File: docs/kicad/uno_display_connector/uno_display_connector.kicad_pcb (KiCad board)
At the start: 2 copper layers, 3 parts, among them J1 Conn_01x08, J2 Conn_01x08, U1 uno_display

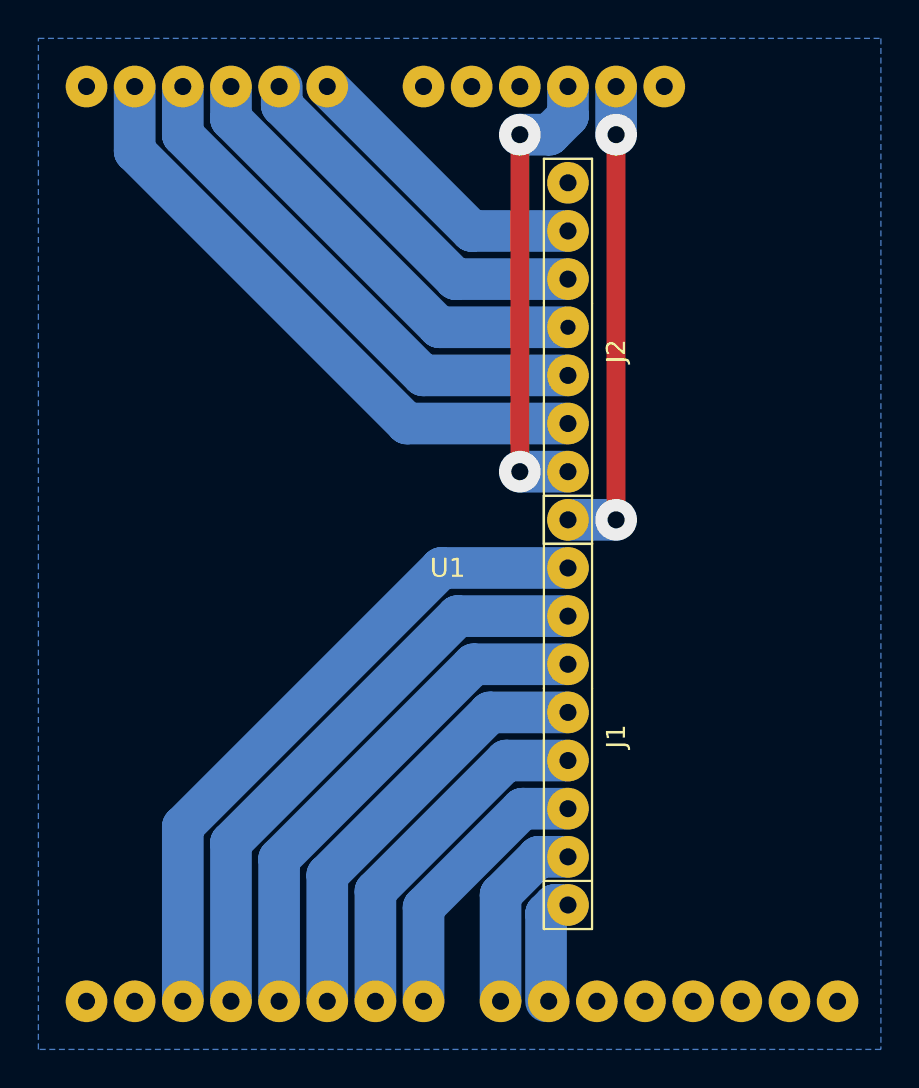
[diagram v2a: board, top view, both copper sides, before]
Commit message: BUILD new combined mother_board and uno_display_connector. PRINT new display_frame.
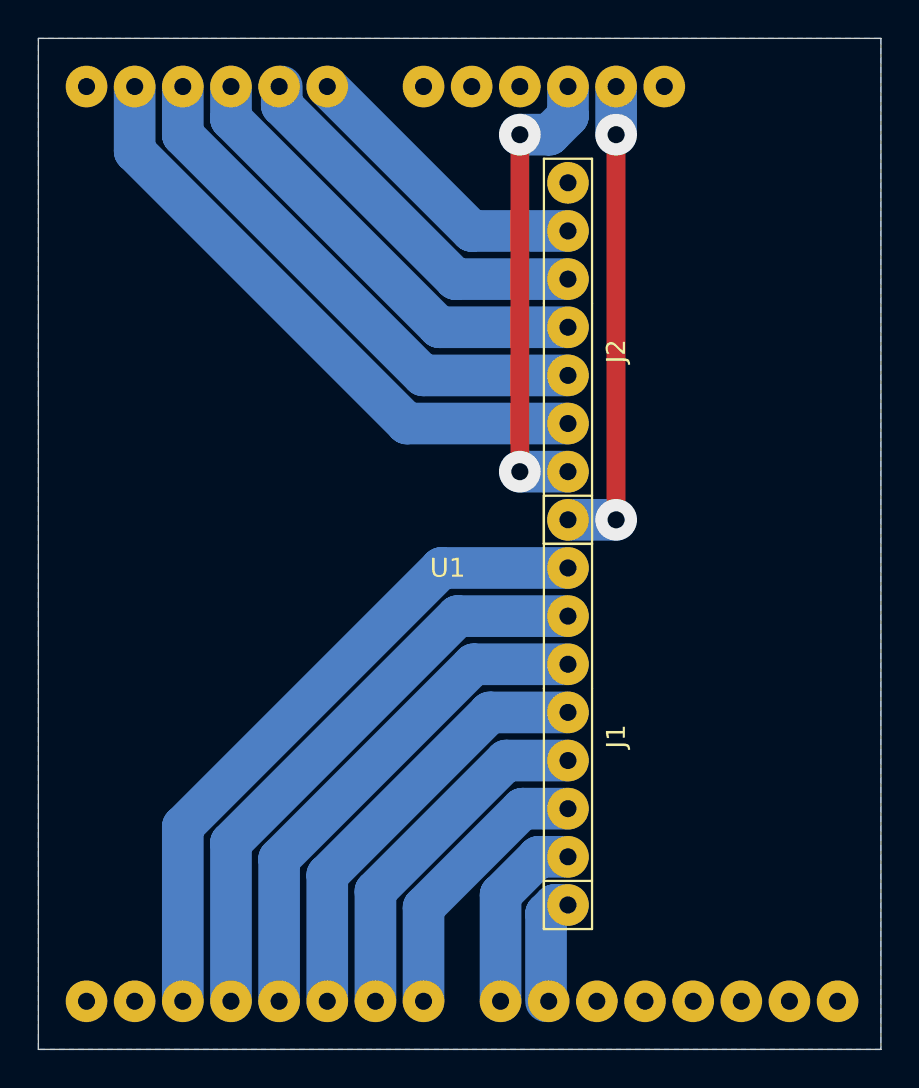
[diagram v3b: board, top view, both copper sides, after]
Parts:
- J1, J2: footprint cnc3018-PCB:my8Pin -> 0_my_footprints:my8Pin
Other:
- board outline added: 44.5 x 53.3 mm
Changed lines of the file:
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@@
   (general
     (thickness 1.6)
-    (drawings 1)
+    (drawings 7)
     (tracks 52)
     (zones 0)
@@
     (add_net "Net-(U1-Pad28)")
   )
-  (module cnc3018-PCB:my8Pin (layer F.Cu)
+  (module 0_my_footprints:my8Pin (layer F.Cu)
     (at 27.94 -15.24 90)
     (fp_text reference J1 (at 1.27 2.54 90) (layer F.SilkS)
@@
     (fp_line (start -8.89 -1.27) (end -6.35 -1.27) (layer F.SilkS) (width 0.12))
     (fp_line (start -6.35 -1.27) (end -6.35 1.27) (layer F.SilkS) (width 0.12))
+    (pad 8 thru_hole circle (at 10.16 0 90) (size 2.2 2.2) (drill 0.9) (layers *.Cu *.Mask)
+      (net 8 LCD_D2))
+    (pad 7 thru_hole circle (at 7.62 0 90) (size 2.2 2.2) (drill 0.9) (layers *.Cu *.Mask)
+      (net 7 LCD_D3))
+    (pad 6 thru_hole circle (at 5.08 0 90) (size 2.2 2.2) (drill 0.9) (layers *.Cu *.Mask)
+      (net 6 LCD_D4))
+    (pad 5 thru_hole circle (at 2.54 0 90) (size 2.2 2.2) (drill 0.9) (layers *.Cu *.Mask)
+      (net 5 LCD_D5))
+    (pad 4 thru_hole circle (at 0 0 90) (size 2.2 2.2) (drill 0.9) (layers *.Cu *.Mask)
+      (net 4 LCD_D6))
+    (pad 3 thru_hole circle (at -2.54 0 90) (size 2.2 2.2) (drill 0.9) (layers *.Cu *.Mask)
+      (net 3 LCD_D7))
+    (pad 2 thru_hole circle (at -5.08 0 90) (size 2.2 2.2) (drill 0.9) (layers *.Cu *.Mask)
+      (net 2 LCD_D0))
     (pad 1 thru_hole circle (at -7.62 0 90) (size 2.2 2.2) (drill 0.9) (layers *.Cu *.Mask)
       (net 1 LCD_D1))
-    (pad 2 thru_hole circle (at -5.08 0 90) (size 2.2 2.2) (drill 0.9) (layers *.Cu *.Mask)
-      (net 2 LCD_D0))
-    (pad 3 thru_hole circle (at -2.54 0 90) (size 2.2 2.2) (drill 0.9) (layers *.Cu *.Mask)
-      (net 3 LCD_D7))
-    (pad 4 thru_hole circle (at 0 0 90) (size 2.2 2.2) (drill 0.9) (layers *.Cu *.Mask)
-      (net 4 LCD_D6))
-    (pad 5 thru_hole circle (at 2.54 0 90) (size 2.2 2.2) (drill 0.9) (layers *.Cu *.Mask)
-      (net 5 LCD_D5))
-    (pad 6 thru_hole circle (at 5.08 0 90) (size 2.2 2.2) (drill 0.9) (layers *.Cu *.Mask)
-      (net 6 LCD_D4))
-    (pad 7 thru_hole circle (at 7.62 0 90) (size 2.2 2.2) (drill 0.9) (layers *.Cu *.Mask)
-      (net 7 LCD_D3))
-    (pad 8 thru_hole circle (at 10.16 0 90) (size 2.2 2.2) (drill 0.9) (layers *.Cu *.Mask)
-      (net 8 LCD_D2))
-  )
-  (module cnc3018-PCB:my8Pin (layer F.Cu)
+  )
+  (module 0_my_footprints:my8Pin (layer F.Cu)
     (at 27.94 -35.56 90)
     (fp_text reference J2 (at 1.27 2.54 90) (layer F.SilkS)
@@
       (effects (font (size 1 1) (thickness 0.15)))
     )
+    (fp_line (start 11.43 1.27) (end 3.81 1.27) (layer F.SilkS) (width 0.12))
+    (fp_line (start 11.43 -1.27) (end 11.43 1.27) (layer F.SilkS) (width 0.12))
+    (fp_line (start 3.81 -1.27) (end 11.43 -1.27) (layer F.SilkS) (width 0.12))
+    (fp_line (start -8.89 -1.27) (end -8.89 1.27) (layer F.SilkS) (width 0.12))
+    (fp_line (start -8.89 1.27) (end 3.81 1.27) (layer F.SilkS) (width 0.12))
+    (fp_line (start 3.81 -1.27) (end -8.89 -1.27) (layer F.SilkS) (width 0.12))
+    (fp_line (start -8.89 -1.27) (end -6.35 -1.27) (layer F.SilkS) (width 0.12))
     (fp_line (start -6.35 -1.27) (end -6.35 1.27) (layer F.SilkS) (width 0.12))
-    (fp_line (start -8.89 -1.27) (end -6.35 -1.27) (layer F.SilkS) (width 0.12))
-    (fp_line (start 3.81 -1.27) (end -8.89 -1.27) (layer F.SilkS) (width 0.12))
-    (fp_line (start -8.89 1.27) (end 3.81 1.27) (layer F.SilkS) (width 0.12))
-    (fp_line (start -8.89 -1.27) (end -8.89 1.27) (layer F.SilkS) (width 0.12))
-    (fp_line (start 3.81 -1.27) (end 11.43 -1.27) (layer F.SilkS) (width 0.12))
-    (fp_line (start 11.43 -1.27) (end 11.43 1.27) (layer F.SilkS) (width 0.12))
-    (fp_line (start 11.43 1.27) (end 3.81 1.27) (layer F.SilkS) (width 0.12))
     (pad 8 thru_hole circle (at 10.16 0 90) (size 2.2 2.2) (drill 0.9) (layers *.Cu *.Mask)
       (net 9 GND))
@@
     (pad 6 thru_hole circle (at 5.08 0 90) (size 2.2 2.2) (drill 0.9) (layers *.Cu *.Mask)
       (net 12 LCD_WR))
-    (pad 5 thru_hole circle (at 2.54 0 90) (size 2.2 2.2) (drill 0.8) (layers *.Cu *.Mask)
+    (pad 5 thru_hole circle (at 2.54 0 90) (size 2.2 2.2) (drill 0.9) (layers *.Cu *.Mask)
       (net 13 LCD_RS))
     (pad 4 thru_hole circle (at 0 0 90) (size 2.2 2.2) (drill 0.9) (layers *.Cu *.Mask)
@@
     )
   )
+  (gr_line (start 44.45 -53.34) (end 0 -53.34) (layer Edge.Cuts) (width 0.05))
+  (gr_line (start 44.45 0) (end 44.45 -53.34) (layer Edge.Cuts) (width 0.05))
+  (gr_line (start 0 0) (end 44.45 0) (layer Edge.Cuts) (width 0.05))
+  (gr_line (start 0 -53.34) (end 0 0) (layer Edge.Cuts) (width 0.05))
+  (dimension 53.34 (width 0.15) (layer Dwgs.User)
+    (gr_text "53.340 mm" (at -13.364999 -26.67 270) (layer Dwgs.User)
+      (effects (font (size 1 1) (thickness 0.15)))
+    )
+    (feature1 (pts (xy 0 0) (xy -12.65142 0)))
+    (feature2 (pts (xy 0 -53.34) (xy -12.65142 -53.34)))
+    (crossbar (pts (xy -12.064999 -53.34) (xy -12.064999 0)))
+    (arrow1a (pts (xy -12.064999 0) (xy -12.65142 -1.126504)))
+    (arrow1b (pts (xy -12.064999 0) (xy -11.478578 -1.126504)))
+    (arrow2a (pts (xy -12.064999 -53.34) (xy -12.65142 -52.213496)))
+    (arrow2b (pts (xy -12.064999 -53.34) (xy -11.478578 -52.213496)))
+  )
+  (dimension 44.45 (width 0.15) (layer Dwgs.User)
+    (gr_text "44.450 mm" (at 22.225 7.014999) (layer Dwgs.User)
+      (effects (font (size 1 1) (thickness 0.15)))
+    )
+    (feature1 (pts (xy 44.45 0) (xy 44.45 6.30142)))
+    (feature2 (pts (xy 0 0) (xy 0 6.30142)))
+    (crossbar (pts (xy 0 5.714999) (xy 44.45 5.714999)))
+    (arrow1a (pts (xy 44.45 5.714999) (xy 43.323496 6.30142)))
+    (arrow1b (pts (xy 44.45 5.714999) (xy 43.323496 5.128578)))
+    (arrow2a (pts (xy 0 5.714999) (xy 1.126504 6.30142)))
+    (arrow2b (pts (xy 0 5.714999) (xy 1.126504 5.128578)))
+  )
   (gr_text "NOTE that LCD_D0 and LCD_D1 are switched\nwhile soldering the wires onto this connector so  \nALL DATA LINES COME OUT IN ORDER on the\nother end as REQUIRED by the mother board!!!" (at 35.56 -17.145) (layer Dwgs.User)

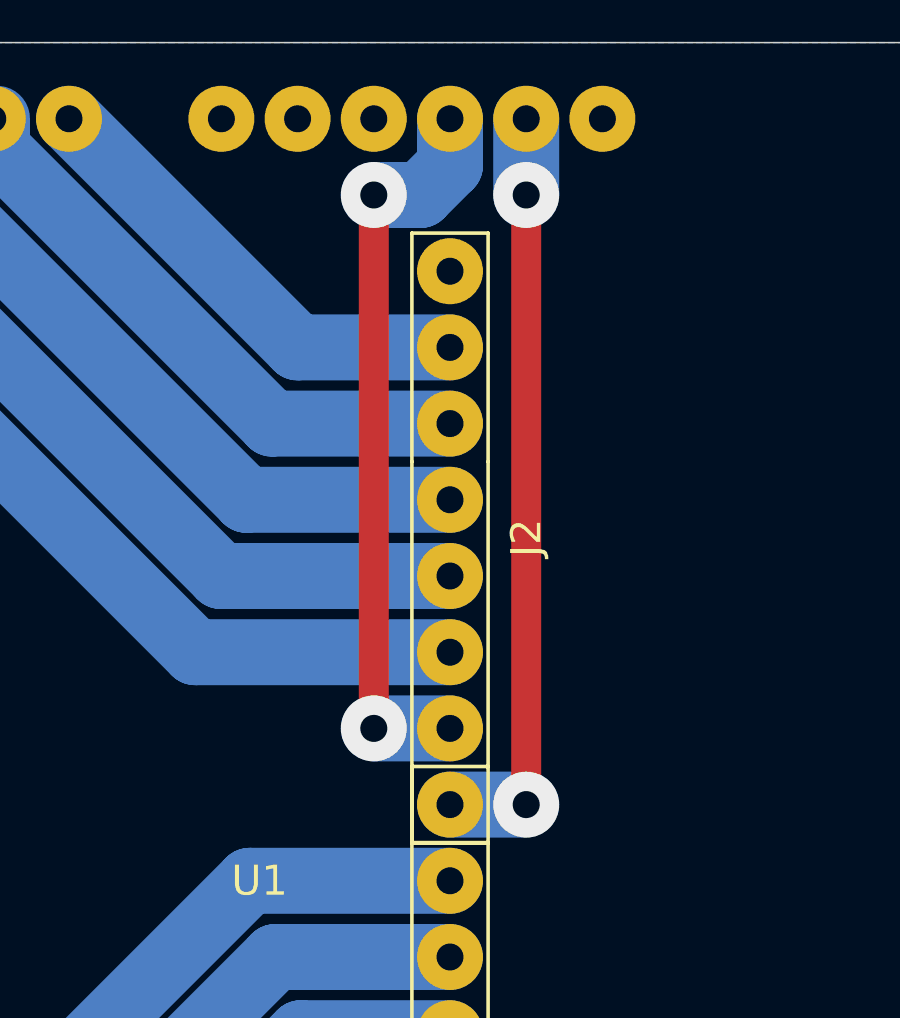
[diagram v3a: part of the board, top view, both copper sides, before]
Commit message: AFTER BUILD NEW PCBs - corrected display connector pins; removed old combined plot and gcode file
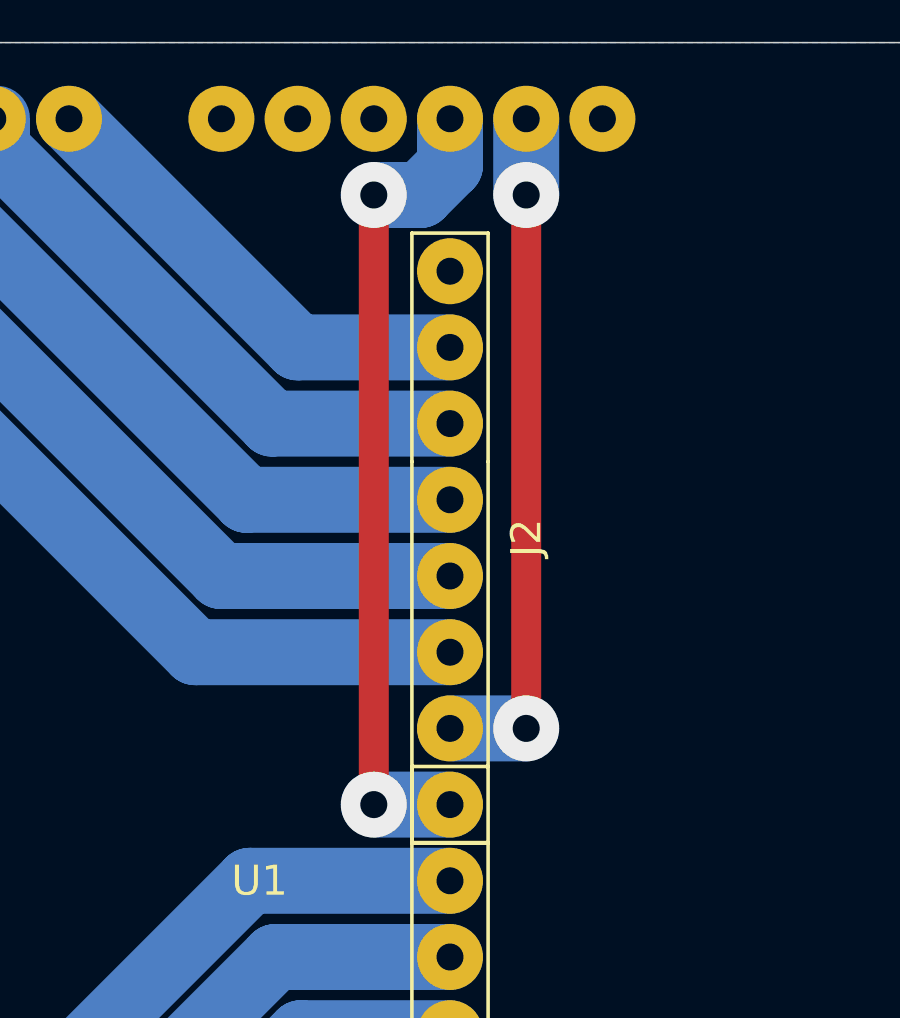
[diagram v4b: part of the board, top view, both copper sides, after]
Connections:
- J2 pad 1: +3V3 -> +5V
- J2 pad 2: +5V -> +3V3
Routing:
- net +5V: track 24.8 -> 27.4 mm
- net +3V3: track 25.4 -> 22.9 mm
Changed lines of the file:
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@@
   )
   (setup
-    (last_trace_width 0.25)
+    (last_trace_width 1)
     (user_trace_width 1)
     (user_trace_width 2)
@@
       (effects (font (size 1 1) (thickness 0.15)))
     )
+    (fp_line (start -6.35 -1.27) (end -6.35 1.27) (layer F.SilkS) (width 0.12))
+    (fp_line (start -8.89 -1.27) (end -6.35 -1.27) (layer F.SilkS) (width 0.12))
+    (fp_line (start 3.81 -1.27) (end -8.89 -1.27) (layer F.SilkS) (width 0.12))
+    (fp_line (start -8.89 1.27) (end 3.81 1.27) (layer F.SilkS) (width 0.12))
+    (fp_line (start -8.89 -1.27) (end -8.89 1.27) (layer F.SilkS) (width 0.12))
+    (fp_line (start 3.81 -1.27) (end 11.43 -1.27) (layer F.SilkS) (width 0.12))
+    (fp_line (start 11.43 -1.27) (end 11.43 1.27) (layer F.SilkS) (width 0.12))
     (fp_line (start 11.43 1.27) (end 3.81 1.27) (layer F.SilkS) (width 0.12))
-    (fp_line (start 11.43 -1.27) (end 11.43 1.27) (layer F.SilkS) (width 0.12))
-    (fp_line (start 3.81 -1.27) (end 11.43 -1.27) (layer F.SilkS) (width 0.12))
-    (fp_line (start -8.89 -1.27) (end -8.89 1.27) (layer F.SilkS) (width 0.12))
-    (fp_line (start -8.89 1.27) (end 3.81 1.27) (layer F.SilkS) (width 0.12))
-    (fp_line (start 3.81 -1.27) (end -8.89 -1.27) (layer F.SilkS) (width 0.12))
-    (fp_line (start -8.89 -1.27) (end -6.35 -1.27) (layer F.SilkS) (width 0.12))
-    (fp_line (start -6.35 -1.27) (end -6.35 1.27) (layer F.SilkS) (width 0.12))
     (pad 8 thru_hole circle (at 10.16 0 90) (size 2.2 2.2) (drill 0.9) (layers *.Cu *.Mask)
       (net 8 LCD_D2))
@@
       (effects (font (size 1 1) (thickness 0.15)))
     )
+    (fp_line (start -6.35 -1.27) (end -6.35 1.27) (layer F.SilkS) (width 0.12))
+    (fp_line (start -8.89 -1.27) (end -6.35 -1.27) (layer F.SilkS) (width 0.12))
+    (fp_line (start 3.81 -1.27) (end -8.89 -1.27) (layer F.SilkS) (width 0.12))
+    (fp_line (start -8.89 1.27) (end 3.81 1.27) (layer F.SilkS) (width 0.12))
+    (fp_line (start -8.89 -1.27) (end -8.89 1.27) (layer F.SilkS) (width 0.12))
+    (fp_line (start 3.81 -1.27) (end 11.43 -1.27) (layer F.SilkS) (width 0.12))
+    (fp_line (start 11.43 -1.27) (end 11.43 1.27) (layer F.SilkS) (width 0.12))
     (fp_line (start 11.43 1.27) (end 3.81 1.27) (layer F.SilkS) (width 0.12))
-    (fp_line (start 11.43 -1.27) (end 11.43 1.27) (layer F.SilkS) (width 0.12))
-    (fp_line (start 3.81 -1.27) (end 11.43 -1.27) (layer F.SilkS) (width 0.12))
-    (fp_line (start -8.89 -1.27) (end -8.89 1.27) (layer F.SilkS) (width 0.12))
-    (fp_line (start -8.89 1.27) (end 3.81 1.27) (layer F.SilkS) (width 0.12))
-    (fp_line (start 3.81 -1.27) (end -8.89 -1.27) (layer F.SilkS) (width 0.12))
-    (fp_line (start -8.89 -1.27) (end -6.35 -1.27) (layer F.SilkS) (width 0.12))
-    (fp_line (start -6.35 -1.27) (end -6.35 1.27) (layer F.SilkS) (width 0.12))
     (pad 8 thru_hole circle (at 10.16 0 90) (size 2.2 2.2) (drill 0.9) (layers *.Cu *.Mask)
       (net 9 GND))
@@
       (net 15 LCD_RST))
     (pad 2 thru_hole circle (at -5.08 0 90) (size 2.2 2.2) (drill 0.9) (layers *.Cu *.Mask)
+      (net 10 +3V3))
+    (pad 1 thru_hole circle (at -7.62 0 90) (size 2.2 2.2) (drill 0.9) (layers *.Cu *.Mask)
       (net 16 +5V))
-    (pad 1 thru_hole circle (at -7.62 0 90) (size 2.2 2.2) (drill 0.9) (layers *.Cu *.Mask)
-      (net 10 +3V3))
   )
   (module 0_my_footprints:unoDisplay (layer F.Cu)
@@
       (effects (font (size 1 1) (thickness 0.15)))
     )
+    (fp_line (start -22.86 -27.94) (end -22.86 25.4) (layer F.Fab) (width 0.12))
+    (fp_line (start -22.86 -27.94) (end 21.59 -27.94) (layer F.Fab) (width 0.12))
+    (fp_line (start 21.59 -27.94) (end 21.59 25.4) (layer F.Fab) (width 0.12))
     (fp_line (start -22.86 25.4) (end 21.59 25.4) (layer F.Fab) (width 0.12))
-    (fp_line (start 21.59 -27.94) (end 21.59 25.4) (layer F.Fab) (width 0.12))
-    (fp_line (start -22.86 -27.94) (end 21.59 -27.94) (layer F.Fab) (width 0.12))
-    (fp_line (start -22.86 -27.94) (end -22.86 25.4) (layer F.Fab) (width 0.12))
     (pad 1 thru_hole circle (at 19.05 -25.4) (size 2.2 2.2) (drill 0.9) (layers *.Cu *.Mask)
       (net 17 "Net-(U1-Pad1)"))
@@
   (segment (start 21.25961 -25.4) (end 27.94 -25.4) (width 2.2) (layer B.Cu) (net 8))
   (segment (start 30.48 -50.8) (end 30.48 -48.26) (width 2.2) (layer B.Cu) (net 10))
-  (segment (start 27.94 -27.94) (end 30.48 -27.94) (width 2.2) (layer B.Cu) (net 10))
-  (via (at 30.48 -27.94) (size 2.2) (drill 0.9) (layers F.Cu B.Cu) (net 10))
+  (segment (start 27.94 -30.48) (end 30.48 -30.48) (width 2.2) (layer B.Cu) (net 10))
+  (via (at 30.48 -30.48) (size 2.2) (drill 0.9) (layers F.Cu B.Cu) (net 10))
   (segment (start 30.48 -48.26) (end 30.48 -48.26) (width 2.2) (layer B.Cu) (net 10))
   (via (at 30.48 -48.26) (size 2.2) (drill 0.9) (layers F.Cu B.Cu) (net 10))
-  (segment (start 30.48 -48.26) (end 30.48 -27.94) (width 1) (layer F.Cu) (net 10))
+  (segment (start 30.48 -30.48) (end 30.48 -48.26) (width 1) (layer F.Cu) (net 10))
   (segment (start 27.94 -43.18) (end 22.86 -43.18) (width 2.2) (layer B.Cu) (net 11))
   (segment (start 22.86 -43.18) (end 15.24 -50.8) (width 2.2) (layer B.Cu) (net 11))
@@
   (segment (start 27.94 -33.02) (end 19.443496 -33.02) (width 2.2) (layer B.Cu) (net 15))
   (segment (start 5.08 -47.383496) (end 5.08 -50.8) (width 2.2) (layer B.Cu) (net 15))
-  (segment (start 27.94 -30.48) (end 25.4 -30.48) (width 2.2) (layer B.Cu) (net 16))
+  (segment (start 27.94 -27.94) (end 25.4 -27.94) (width 2.2) (layer B.Cu) (net 16))
   (segment (start 27.94 -49.244366) (end 26.955634 -48.26) (width 2.2) (layer B.Cu) (net 16))
   (segment (start 27.94 -50.8) (end 27.94 -49.244366) (width 2.2) (layer B.Cu) (net 16))
   (segment (start 26.955634 -48.26) (end 25.4 -48.26) (width 2.2) (layer B.Cu) (net 16))
-  (via (at 25.4 -30.48) (size 2.2) (drill 0.9) (layers F.Cu B.Cu) (net 16))
+  (via (at 25.4 -27.94) (size 2.2) (drill 0.9) (layers F.Cu B.Cu) (net 16))
   (segment (start 25.4 -48.26) (end 25.4 -48.26) (width 2.2) (layer B.Cu) (net 16))
   (via (at 25.4 -48.26) (size 2.2) (drill 0.9) (layers F.Cu B.Cu) (net 16))
-  (segment (start 25.4 -48.26) (end 25.4 -30.48) (width 1) (layer F.Cu) (net 16))
+  (segment (start 25.4 -48.26) (end 25.4 -27.94) (width 1) (layer F.Cu) (net 16))
   (zone (net 9) (net_name GND) (layer B.Cu) (hatch edge 0.508)
     (connect_pads yes (clearance 0.3))
